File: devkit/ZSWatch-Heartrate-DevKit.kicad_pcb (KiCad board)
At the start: 4 copper layers, 45 x 36.9 mm, 49 parts, among them IC401 MIC5365-1.8, IC402 TPS61240, IC403 MCP73832-2-OT, IC404 MAX32664, IC405 MAX86141, IC406 LIS2DS12, J401 I2C, J402 SPI, M401 BM15C, Q401 BSS138, SW401 RESET, SW402 BTN1, X401 CHARGE, X402 BATTERY, X403 DEBUG, Y401 32kHz

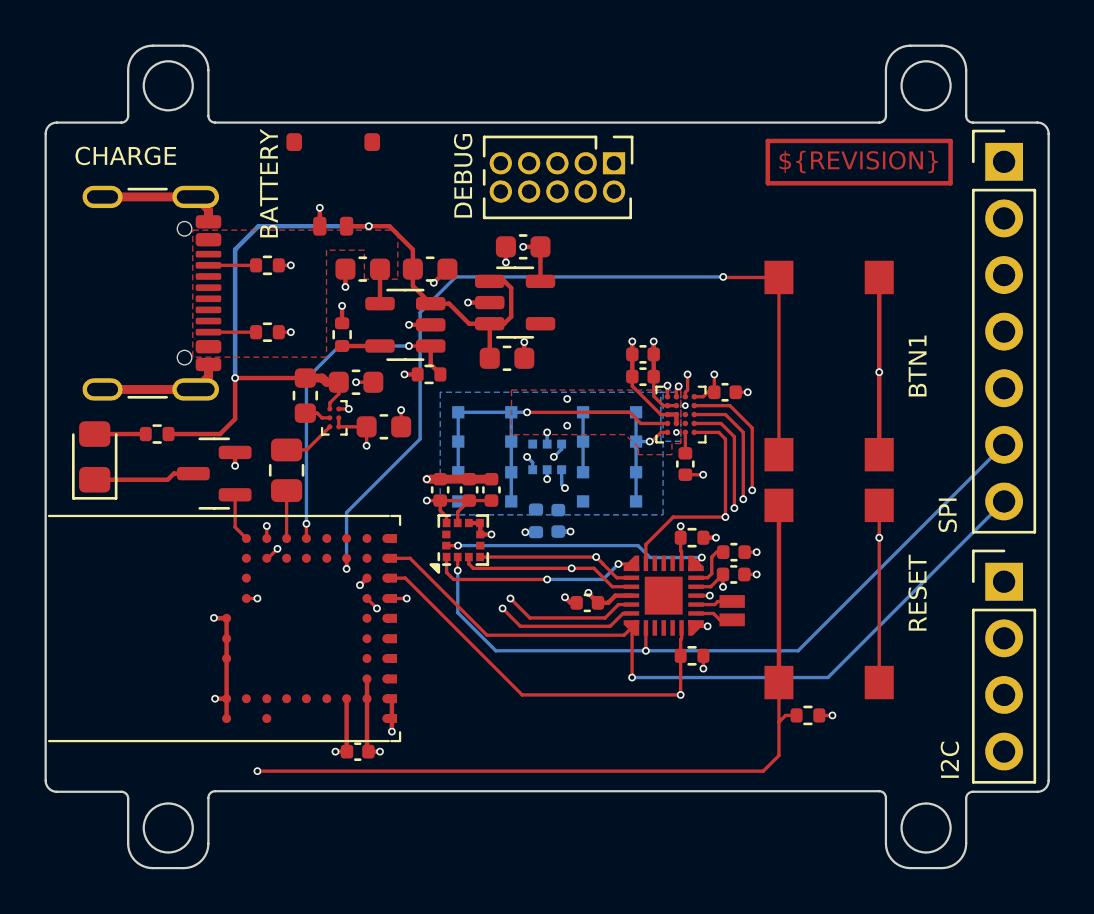
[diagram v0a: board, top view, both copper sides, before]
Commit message: Prepare release
- Set variant to CHECKED
- Remove unused files
- Fix ERC errors
- Fix DRC errors
- Fix different documentation errors
- Fix different path errors for the release build
- Remove Power Sequencing page
- Add PDF_REPORT_ROOT_DIR variable to build
- Add script for CHANGELOG generation

Signed-off-by: Daniel Kampert <DanielKampert@kampis-elektroecke.de>
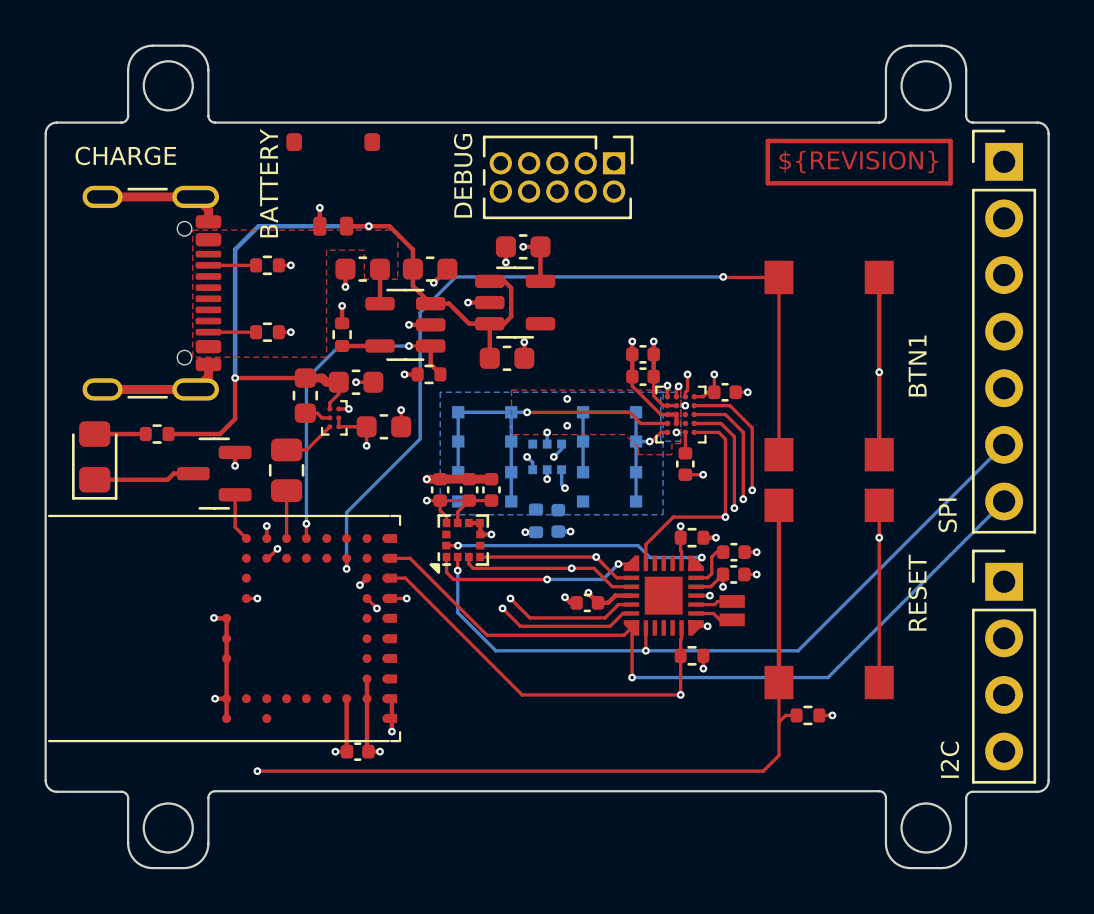
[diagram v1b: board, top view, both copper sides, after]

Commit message: Update outputs (release)
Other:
- board text added: "0.196mm"
- board text added: "0.43mm"
- board text added: "Inner1"
- board text added: "Inner2"
- board text added: "Plane"
- board text added: "Prepreg"
- board text added: "Total thickness: 0.982mm"
- board text removed: "1.51mm"
- board text removed: "Total thickness: 1.6mm"
